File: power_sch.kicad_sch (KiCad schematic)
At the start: 0 parts

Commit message: Draw power schematic.
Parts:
- added C12, C14: 1uF, Capacitor_SMD:C_0603_1608Metric_Pad1.08x0.95mm_HandSolder, symbol Device:C
- added C13, C15: 2.2uF, Capacitor_SMD:C_0603_1608Metric_Pad1.08x0.95mm_HandSolder, symbol Device:C
- added F2, F3: 500mA, Resistor_SMD:R_1206_3216Metric_Pad1.30x1.75mm_HandSolder, symbol Device:Fuse
- added NT1, NT2: NetTie_2, symbol Device:NetTie_2
- added Q6, Q7: RUM002N05T2L, Package_TO_SOT_SMD:SOT-723, symbol Device:Q_NMOS
- added R21, R23: 1.5M, Resistor_SMD:R_0603_1608Metric_Pad0.98x0.95mm_HandSolder, symbol Device:R
- added R22, R24: 1.2M, Resistor_SMD:R_0603_1608Metric_Pad0.98x0.95mm_HandSolder, symbol Device:R
- added R25, R26, R27, R28: 10K, Resistor_SMD:R_0603_1608Metric_Pad0.98x0.95mm_HandSolder, symbol Device:R
- added U3, U4: TPS7A2601DRVR, custom:DRV0006A, symbol custom:TPS7A2601DRVR
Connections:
- new net: C13.2, F2.1, R21.2, U3.1 (OUT)
- new net: R23.1, R24.2, U4.2 (FB_NC)
- new net: C15.2, F3.1, R23.2, U4.1 (OUT)
- new net: Q6.1 (G), Q7.3 (D), R25.1
- new net: R21.1, R22.2, U3.2 (FB_NC)
- new net: Q6.3 (D), R26.1, U4.4 (EN)
- new net: Q7.1 (G), R27.2, R28.1
- new net GNDA: C14.1, C15.1, NT2.2, R24.1, U4.5 (GND), U4.7 (PAD)
- new net GNDD: C12.1, C13.1, NT1.2, Q6.2 (S), Q7.2 (S), R22.1, R27.1, U3.5 (GND), U3.7 (PAD)
- new net GNDPWR: NT1.1, NT2.1
- new net Van+: F3.2
- new net Vin+: C12.2, C14.2, R25.2, R26.2, U3.4 (EN), U3.6 (IN), U4.6 (IN)
- new net Vmcu+: F2.2
- new net enable_an: R28.2
- no-connect marks 0 -> 2
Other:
- note added: "FET will disable the LDO at Vgs threshold (0.3,1)V."

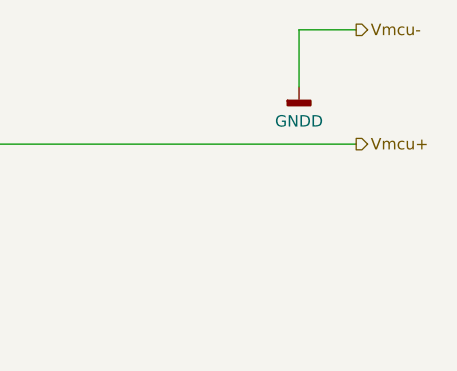
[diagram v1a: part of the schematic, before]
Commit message: Change BJT to FET in MCU. Add pinout.
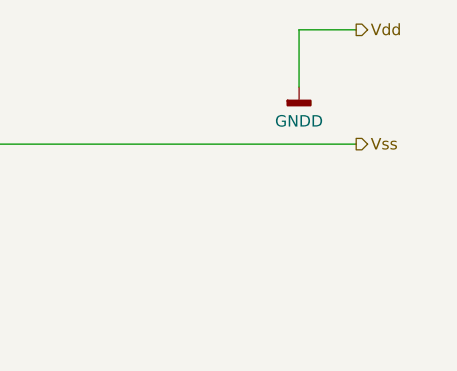
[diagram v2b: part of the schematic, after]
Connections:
- net Vmcu+ renamed Vss
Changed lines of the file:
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@@
 		)
 	)
-	(hierarchical_label "Vmcu+"
+	(hierarchical_label "Vss"
 		(shape output)
 		(at 266.7 44.45 0)
@@
 		)
 	)
-	(hierarchical_label "Vmcu-"
+	(hierarchical_label "Vdd"
 		(shape output)
 		(at 266.7 31.75 0)

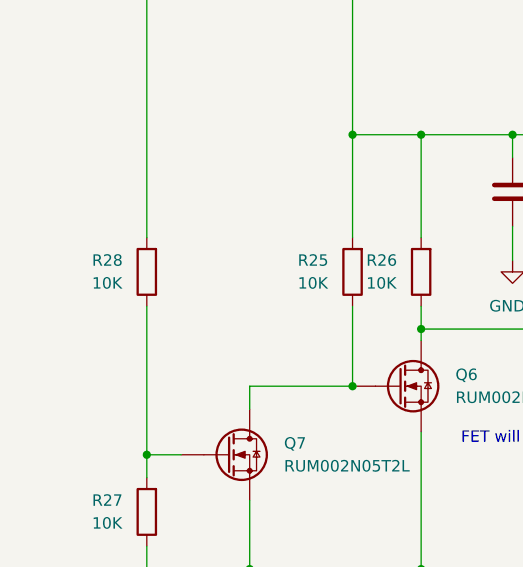
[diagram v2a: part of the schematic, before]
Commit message: Add analog schematic and refine wiring on top.
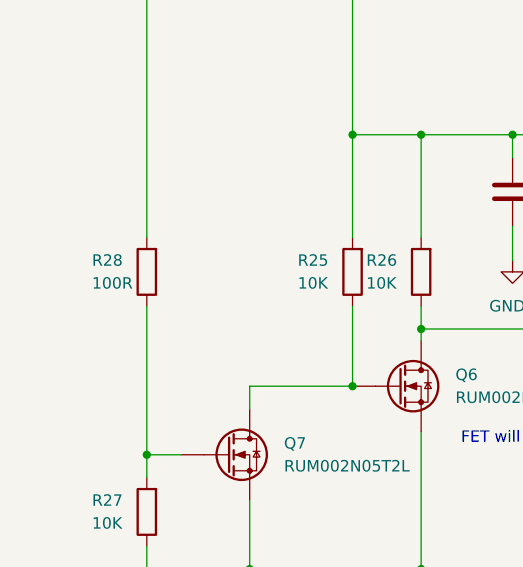
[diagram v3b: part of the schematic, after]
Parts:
- R28: value 10K -> 100R
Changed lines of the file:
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@@
 			)
 		)
-		(property "Value" "10K"
+		(property "Value" "100R"
 			(at 20.574 107.95 0)
 			(show_name no)

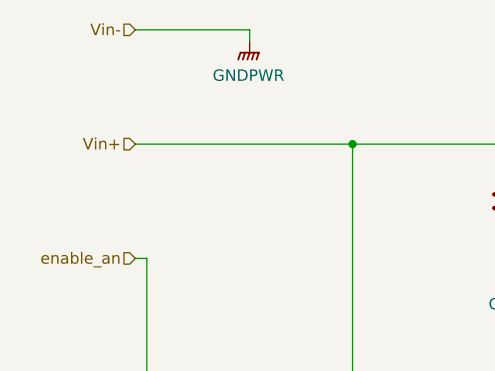
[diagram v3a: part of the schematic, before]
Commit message: Add charger, battery cell.
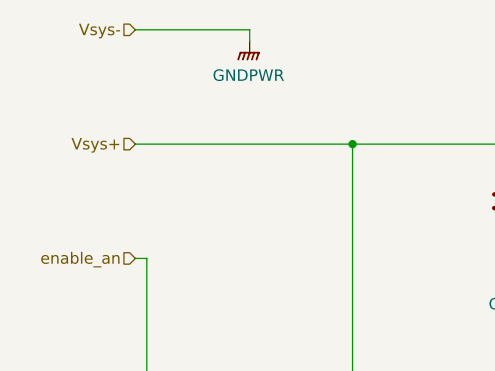
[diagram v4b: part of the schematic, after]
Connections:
- net Vin+ renamed Vsys+
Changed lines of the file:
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@@
 		)
 	)
-	(hierarchical_label "Vin-"
+	(hierarchical_label "Vsys-"
 		(shape input)
 		(at 25.4 31.75 180)
@@
 		)
 	)
-	(hierarchical_label "Vin+"
+	(hierarchical_label "Vsys+"
 		(shape input)
 		(at 25.4 44.45 180)

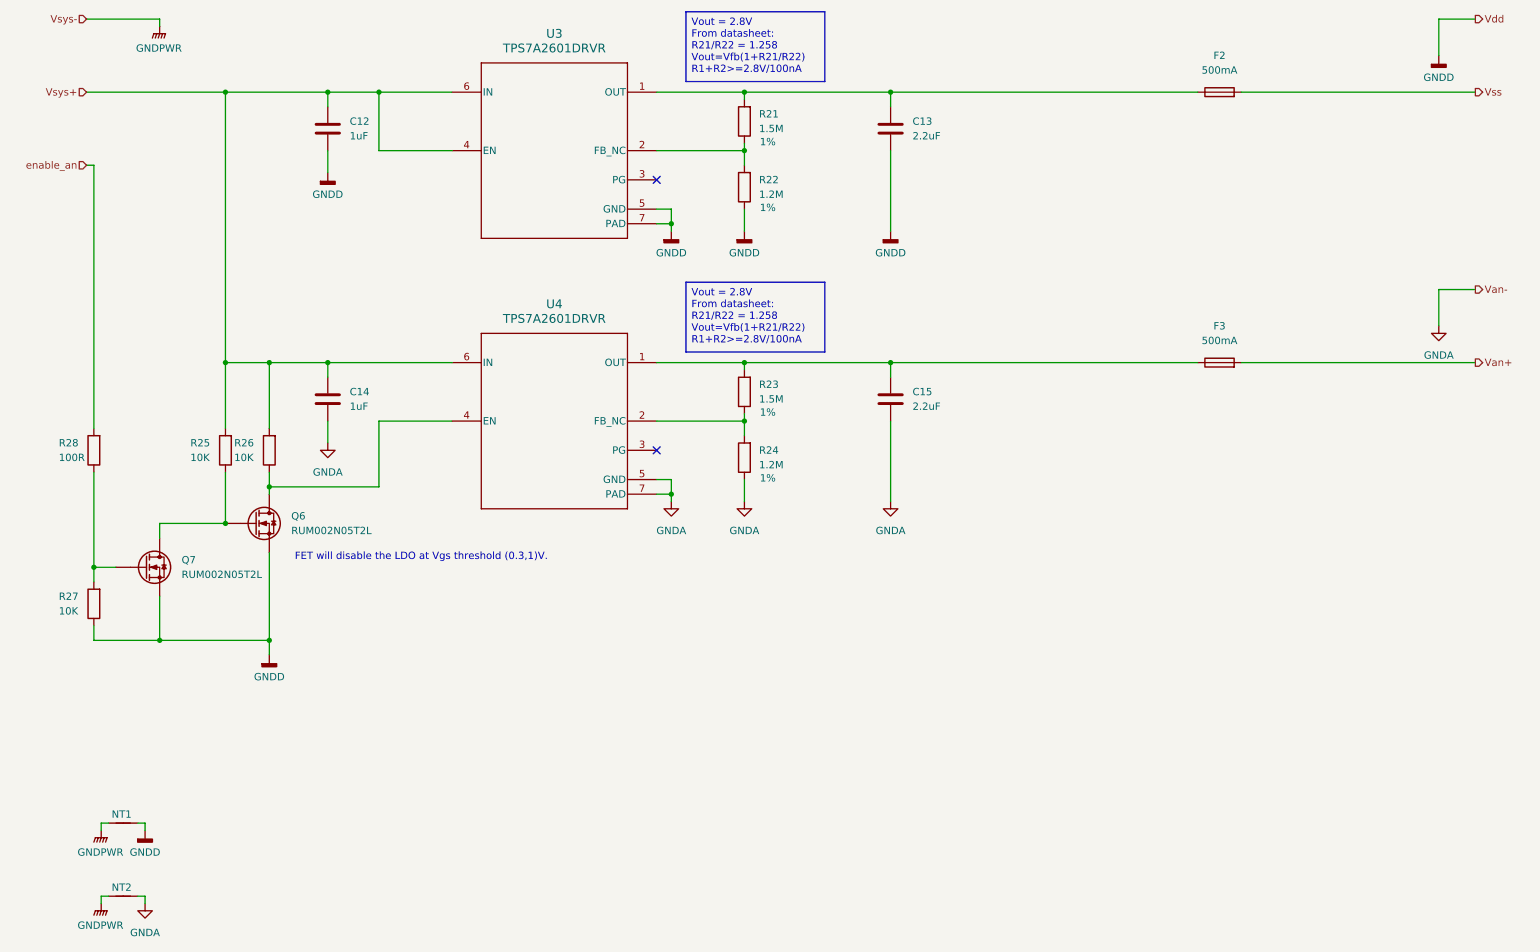
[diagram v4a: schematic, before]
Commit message: Add console port.
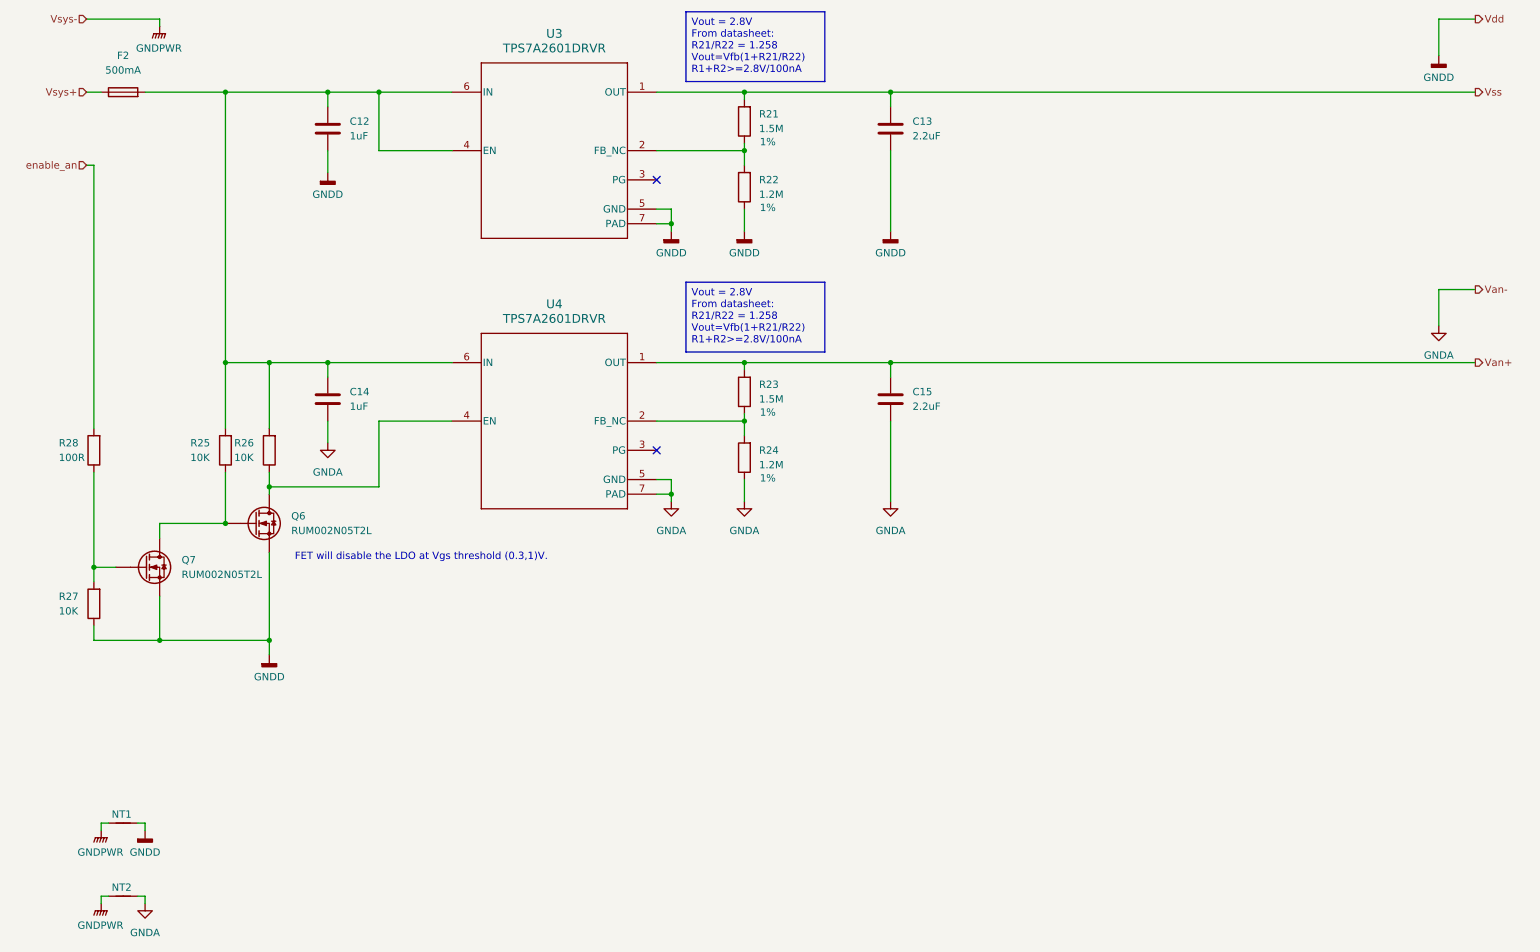
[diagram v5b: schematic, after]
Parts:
- removed F3: 500mA, Resistor_SMD:R_1206_3216Metric_Pad1.30x1.75mm_HandSolder, symbol Device:Fuse
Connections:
- net Van+: now also C15.2, R23.2, U4.1 (OUT)
- net Vss: now also C13.2, R21.2, U3.1 (OUT); no longer F2.2
- net Vsys+: now also F2.1; no longer C12.2, C14.2, R25.2, R26.2, U3.4 (EN), U3.6 (IN), U4.6 (IN)
- new net: C12.2, C14.2, F2.2, R25.2, R26.2, U3.4 (EN), U3.6 (IN), U4.6 (IN)
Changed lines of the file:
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@@
 	(wire
 		(pts
-			(xy 226.06 44.45) (xy 266.7 44.45)
-		)
-		(stroke
-			(width 0)
-			(type default)
-		)
-	)
-	(wire
-		(pts
 			(xy 49.53 44.45) (xy 67.31 44.45)
 		)
@@
 	(wire
 		(pts
-			(xy 165.1 44.45) (xy 218.44 44.45)
+			(xy 165.1 44.45) (xy 266.7 44.45)
 		)
 		(stroke
@@
 	(wire
 		(pts
-			(xy 25.4 44.45) (xy 49.53 44.45)
+			(xy 25.4 44.45) (xy 27.94 44.45)
 		)
 		(stroke
@@
 	(wire
 		(pts
+			(xy 35.56 44.45) (xy 49.53 44.45)
+		)
+		(stroke
+			(width 0)
+			(type default)
+		)
+	)
+	(wire
+		(pts
 			(xy 57.15 113.03) (xy 76.2 113.03)
 		)
@@
 	(wire
 		(pts
-			(xy 165.1 91.44) (xy 218.44 91.44)
+			(xy 165.1 91.44) (xy 266.7 91.44)
 		)
 		(stroke
@@
 	(wire
 		(pts
-			(xy 226.06 91.44) (xy 266.7 91.44)
-		)
-		(stroke
-			(width 0)
-			(type default)
-		)
-	)
-	(wire
-		(pts
 			(xy 139.7 101.6) (xy 139.7 104.14)
 		)
@@
 	)
 	(symbol
-		(lib_id "Device:Fuse")
-		(at 222.25 44.45 90)
+		(lib_id "power:GNDA")
+		(at 67.31 105.41 0)
 		(unit 1)
 		(body_style 1)
@@
 		(dnp no)
 		(fields_autoplaced yes)
-		(property "Reference" "F2"
-			(at 222.25 38.1 90)
+		(property "Reference" "#PWR023"
+			(at 67.31 111.76 0)
+			(hide yes)
 			(show_name no)
 			(do_not_autoplace no)
@@
 			)
 		)
-		(property "Value" "500mA"
-			(at 222.25 40.64 90)
+		(property "Value" "GNDA"
+			(at 67.31 110.49 0)
 			(show_name no)
 			(do_not_autoplace no)
@@
 			)
 		)
-		(property "Footprint" "Resistor_SMD:R_1206_3216Metric_Pad1.30x1.75mm_HandSolder"
-			(at 222.25 46.228 90)
+		(property "Footprint" ""
+			(at 67.31 105.41 0)
 			(hide yes)
 			(show_name no)
@@
 		)
 		(property "Datasheet" ""
-			(at 222.25 44.45 0)
+			(at 67.31 105.41 0)
 			(hide yes)
 			(show_name no)
@@
 			)
 		)
-		(property "Description" "Fuse"
-			(at 222.25 44.45 0)
+		(property "Description" "Power symbol creates a global label with name \"GNDA\" , analog ground"
+			(at 67.31 105.41 0)
 			(hide yes)
 			(show_name no)
@@
 			)
 		)
-		(pin "2"
-		)
 		(pin "1"
 		)
@@
 			(project "MoistureESP"
 				(path "/f2b9f638-139e-46ec-aa60-77c4af989196/49685a81-7509-4241-9c59-8f2ca08912fe"
-					(reference "F2")
+					(reference "#PWR023")
 					(unit 1)
 				)
@@
 	)
 	(symbol
-		(lib_id "power:GNDA")
-		(at 67.31 105.41 0)
+		(lib_id "Device:Fuse")
+		(at 31.75 44.45 90)
 		(unit 1)
 		(body_style 1)
@@
 		(dnp no)
 		(fields_autoplaced yes)
-		(property "Reference" "#PWR023"
-			(at 67.31 111.76 0)
-			(hide yes)
+		(property "Reference" "F2"
+			(at 31.75 38.1 90)
 			(show_name no)
 			(do_not_autoplace no)
@@
 			)
 		)
-		(property "Value" "GNDA"
-			(at 67.31 110.49 0)
+		(property "Value" "500mA"
+			(at 31.75 40.64 90)
 			(show_name no)
 			(do_not_autoplace no)
@@
 			)
 		)
-		(property "Footprint" ""
-			(at 67.31 105.41 0)
+		(property "Footprint" "Resistor_SMD:R_1206_3216Metric_Pad1.30x1.75mm_HandSolder"
+			(at 31.75 46.228 90)
 			(hide yes)
 			(show_name no)
@@
 		)
 		(property "Datasheet" ""
-			(at 67.31 105.41 0)
+			(at 31.75 44.45 0)
 			(hide yes)
 			(show_name no)
@@
 			)
 		)
-		(property "Description" "Power symbol creates a global label with name \"GNDA\" , analog ground"
-			(at 67.31 105.41 0)
+		(property "Description" "Fuse"
+			(at 31.75 44.45 0)
 			(hide yes)
 			(show_name no)
@@
 			)
 		)
+		(pin "2"
+		)
 		(pin "1"
 		)
@@
 			(project "MoistureESP"
 				(path "/f2b9f638-139e-46ec-aa60-77c4af989196/49685a81-7509-4241-9c59-8f2ca08912fe"
-					(reference "#PWR023")
+					(reference "F2")
 					(unit 1)
 				)
@@
 					(unit 1)
 				)
-			)
-		)
-	)
-	(symbol
-		(lib_id "Device:Fuse")
-		(at 222.25 91.44 90)
-		(unit 1)
-		(body_style 1)
-		(exclude_from_sim no)
-		(in_bom yes)
-		(on_board yes)
-		(in_pos_files yes)
-		(dnp no)
-		(fields_autoplaced yes)
-		(property "Reference" "F3"
-			(at 222.25 85.09 90)
-			(show_name no)
-			(do_not_autoplace no)
-			(effects
-				(font
-					(size 1.27 1.27)
-				)
-			)
-		)
-		(property "Value" "500mA"
-			(at 222.25 87.63 90)
-			(show_name no)
-			(do_not_autoplace no)
-			(effects
-				(font
-					(size 1.27 1.27)
-				)
-			)
-		)
-		(property "Footprint" "Resistor_SMD:R_1206_3216Metric_Pad1.30x1.75mm_HandSolder"
-			(at 222.25 93.218 90)
-			(hide yes)
-			(show_name no)
-			(do_not_autoplace no)
-			(effects
-				(font
-					(size 1.27 1.27)
-				)
-			)
-		)
-		(property "Datasheet" ""
-			(at 222.25 91.44 0)
-			(hide yes)
-			(show_name no)
-			(do_not_autoplace no)
-			(effects
-				(font
-					(size 1.27 1.27)
-				)
-			)
-		)
-		(property "Description" "Fuse"
-			(at 222.25 91.44 0)
-			(hide yes)
-			(show_name no)
-			(do_not_autoplace no)
-			(effects
-				(font
-					(size 1.27 1.27)
-				)
-			)
-		)
-		(pin "2"
-		)
-		(pin "1"
-		)
-		(instances
-			(project "MoistureESP"
-				(path "/f2b9f638-139e-46ec-aa60-77c4af989196/49685a81-7509-4241-9c59-8f2ca08912fe"
-					(reference "F3")
-					(unit 1)
-				)

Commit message: Fix issues
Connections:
- net GNDA: no longer C14.1, C15.1, R24.1, U4.5 (GND), U4.7 (PAD)
- net GNDD: no longer C12.1, C13.1, Q6.2 (S), Q7.2 (S), R22.1, R27.1, U3.5 (GND), U3.7 (PAD)
- net GNDPWR: now also C12.1, C13.1, C14.1, C15.1, Q6.2 (S), Q7.2 (S), R22.1, R24.1, R27.1, U3.5 (GND), U3.7 (PAD), U4.5 (GND), U4.7 (PAD)

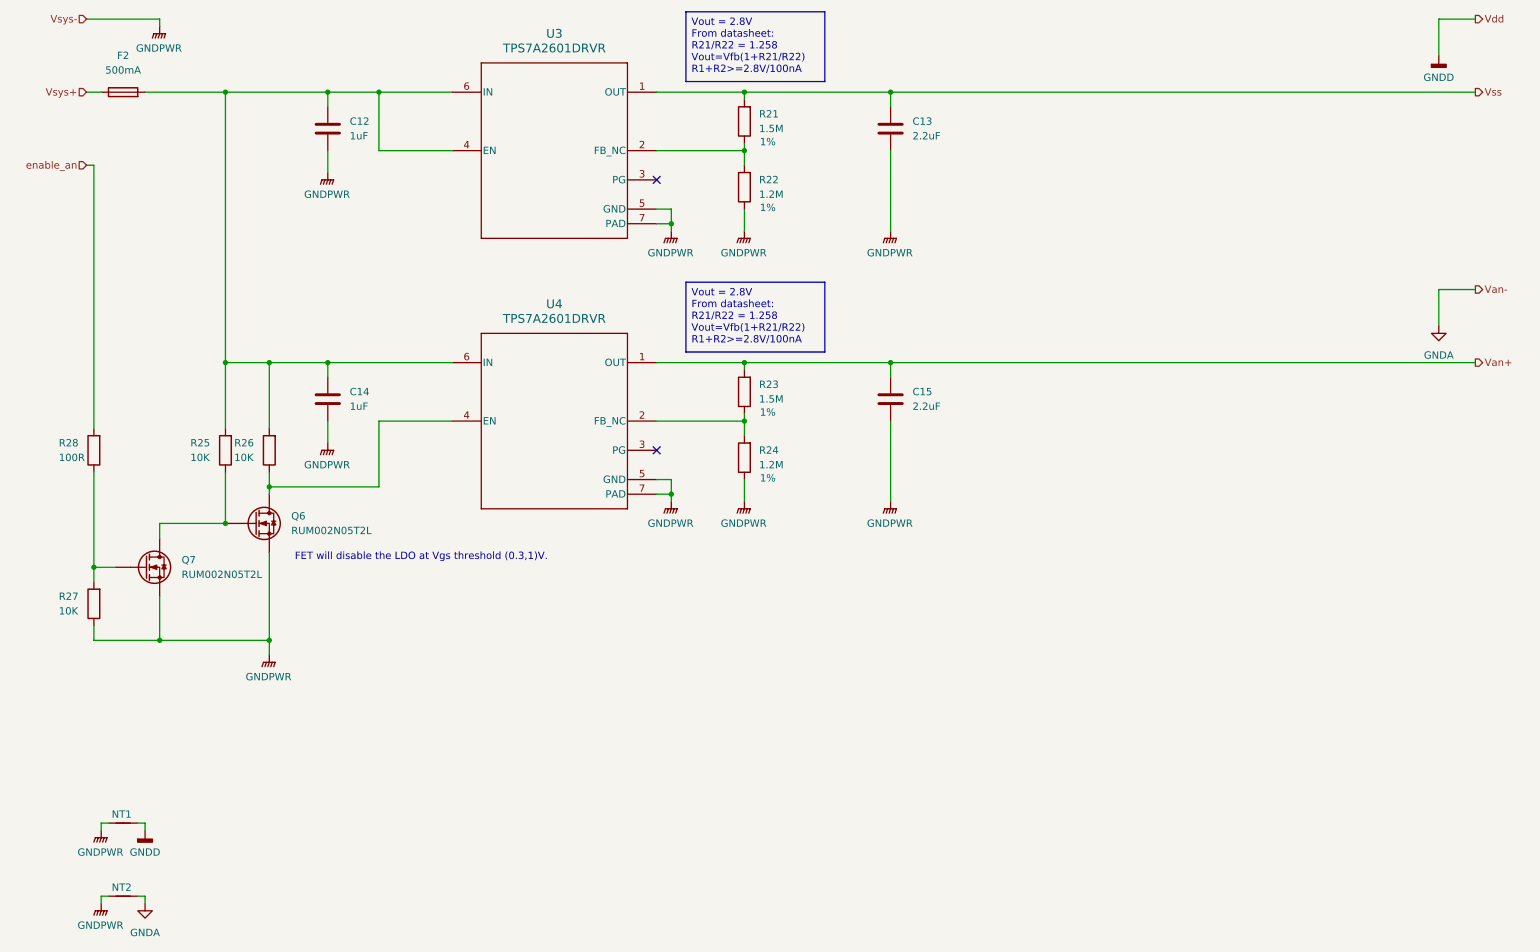
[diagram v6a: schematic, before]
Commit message: Add protected Vbat charger input.
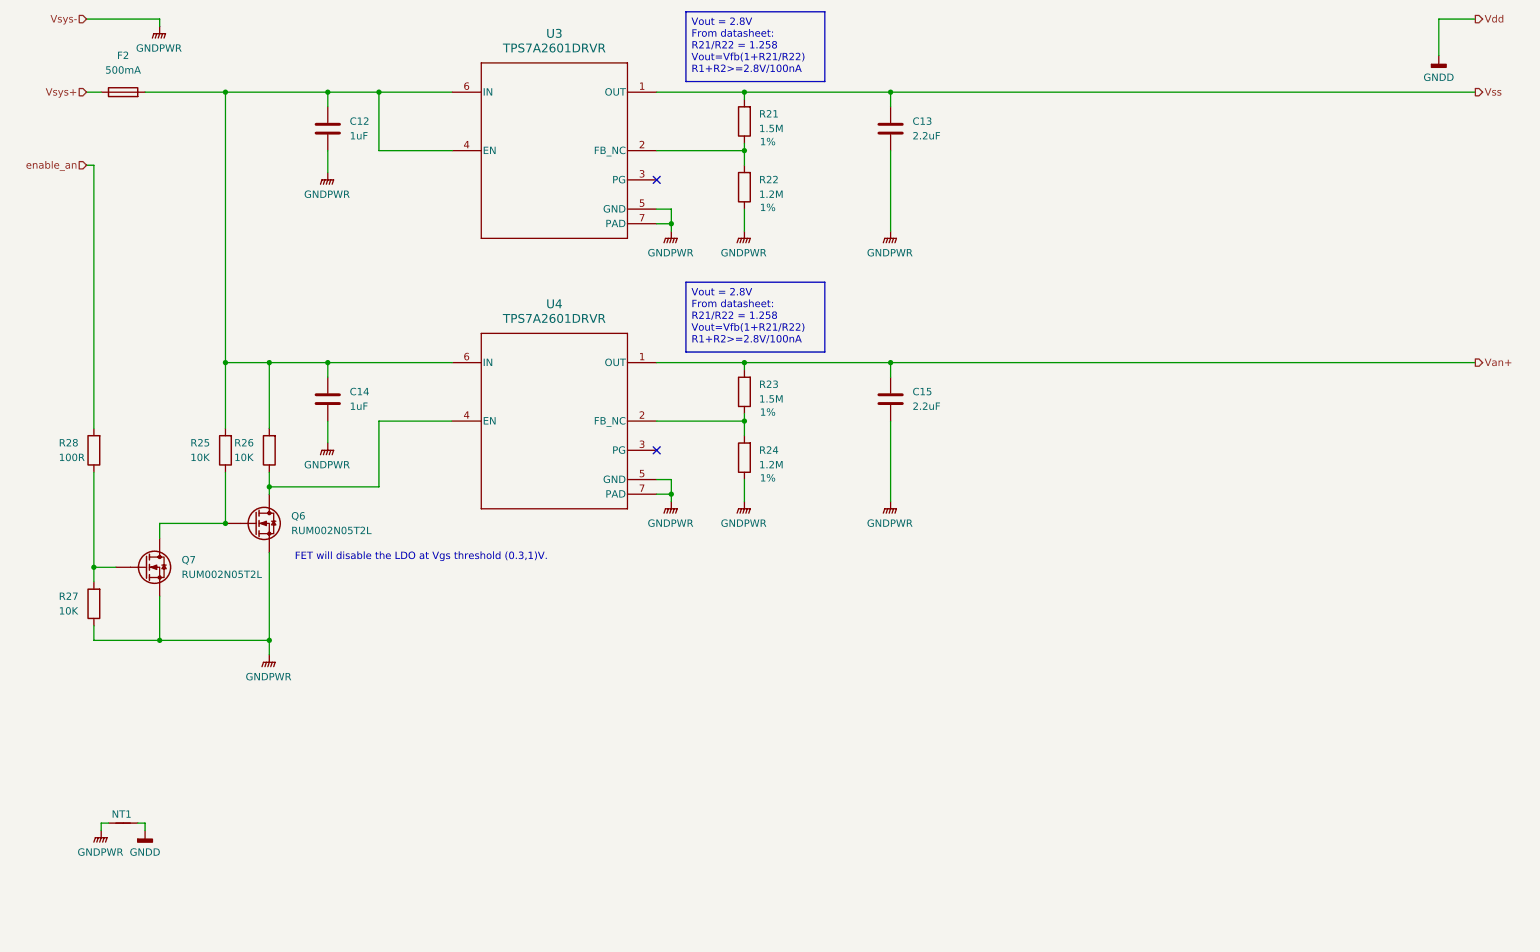
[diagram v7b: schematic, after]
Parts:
- removed NT2: NetTie_2, symbol Device:NetTie_2
